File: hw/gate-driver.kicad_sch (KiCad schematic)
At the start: 7 parts

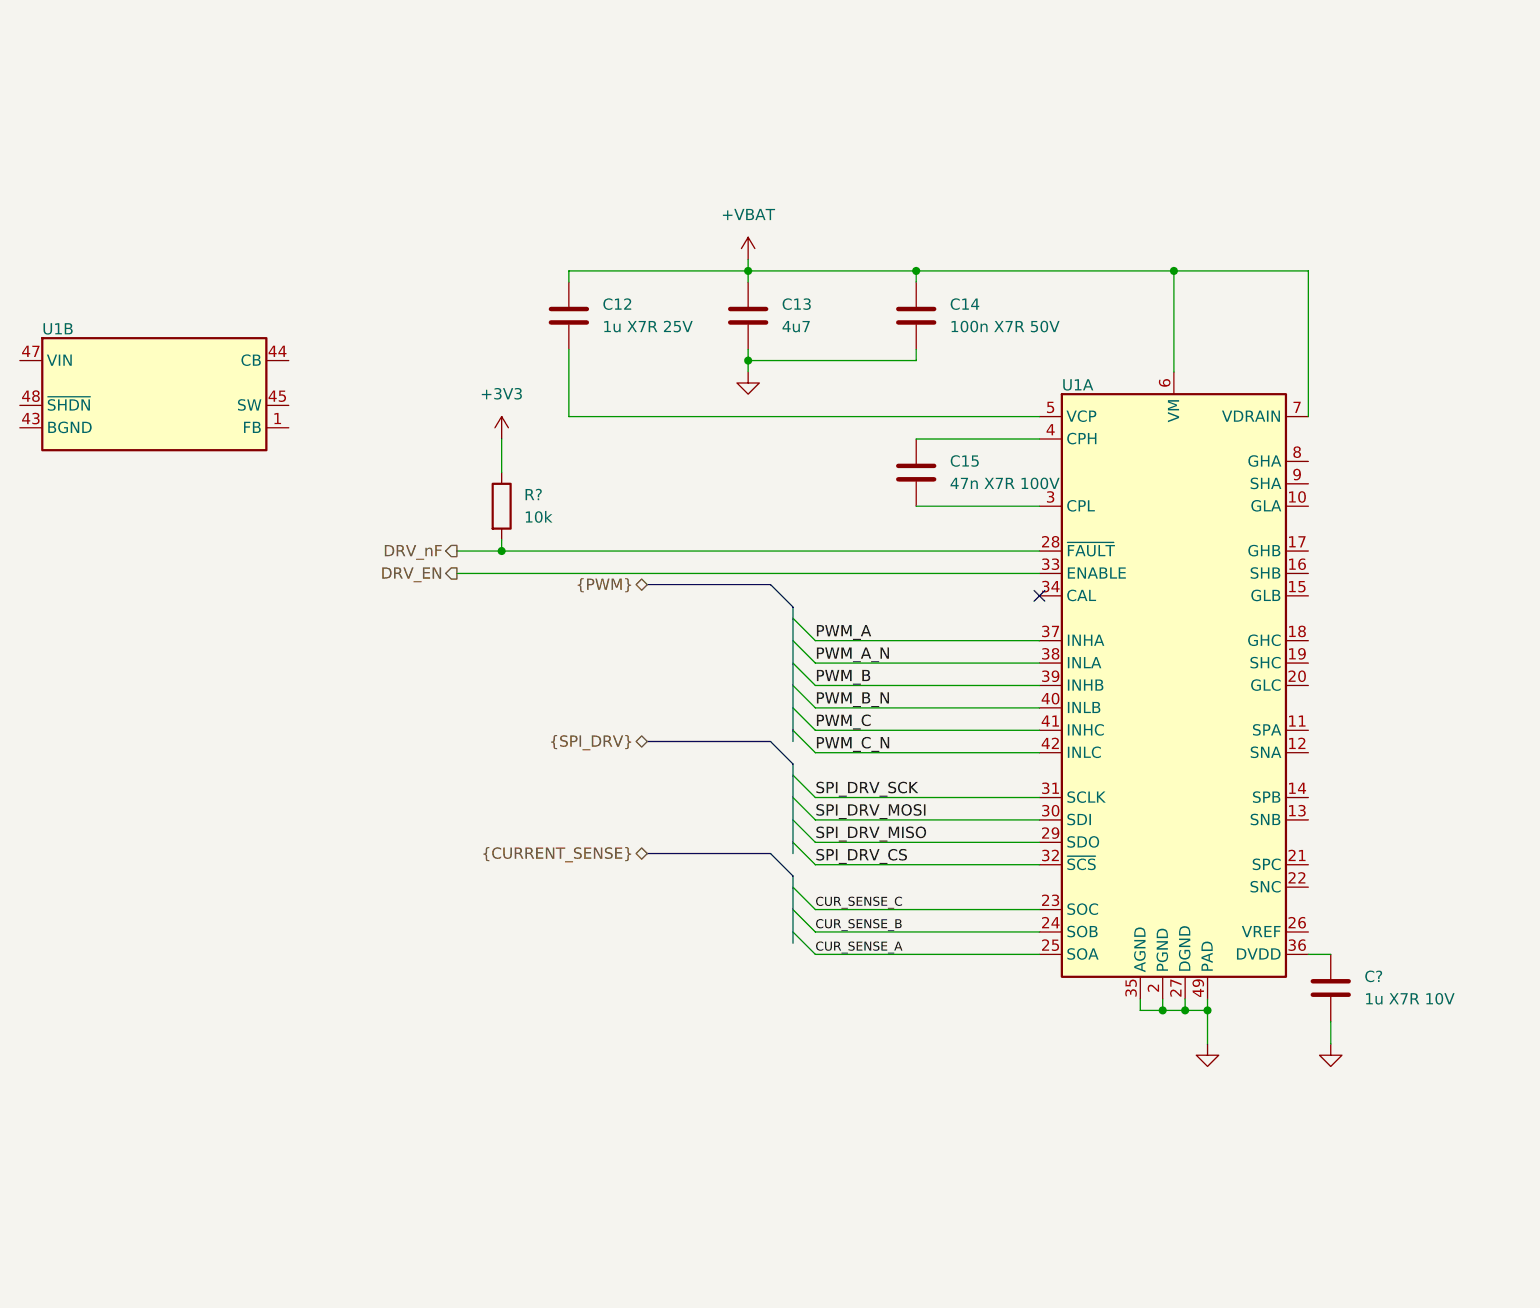
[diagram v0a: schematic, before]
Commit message: add inverter-stage
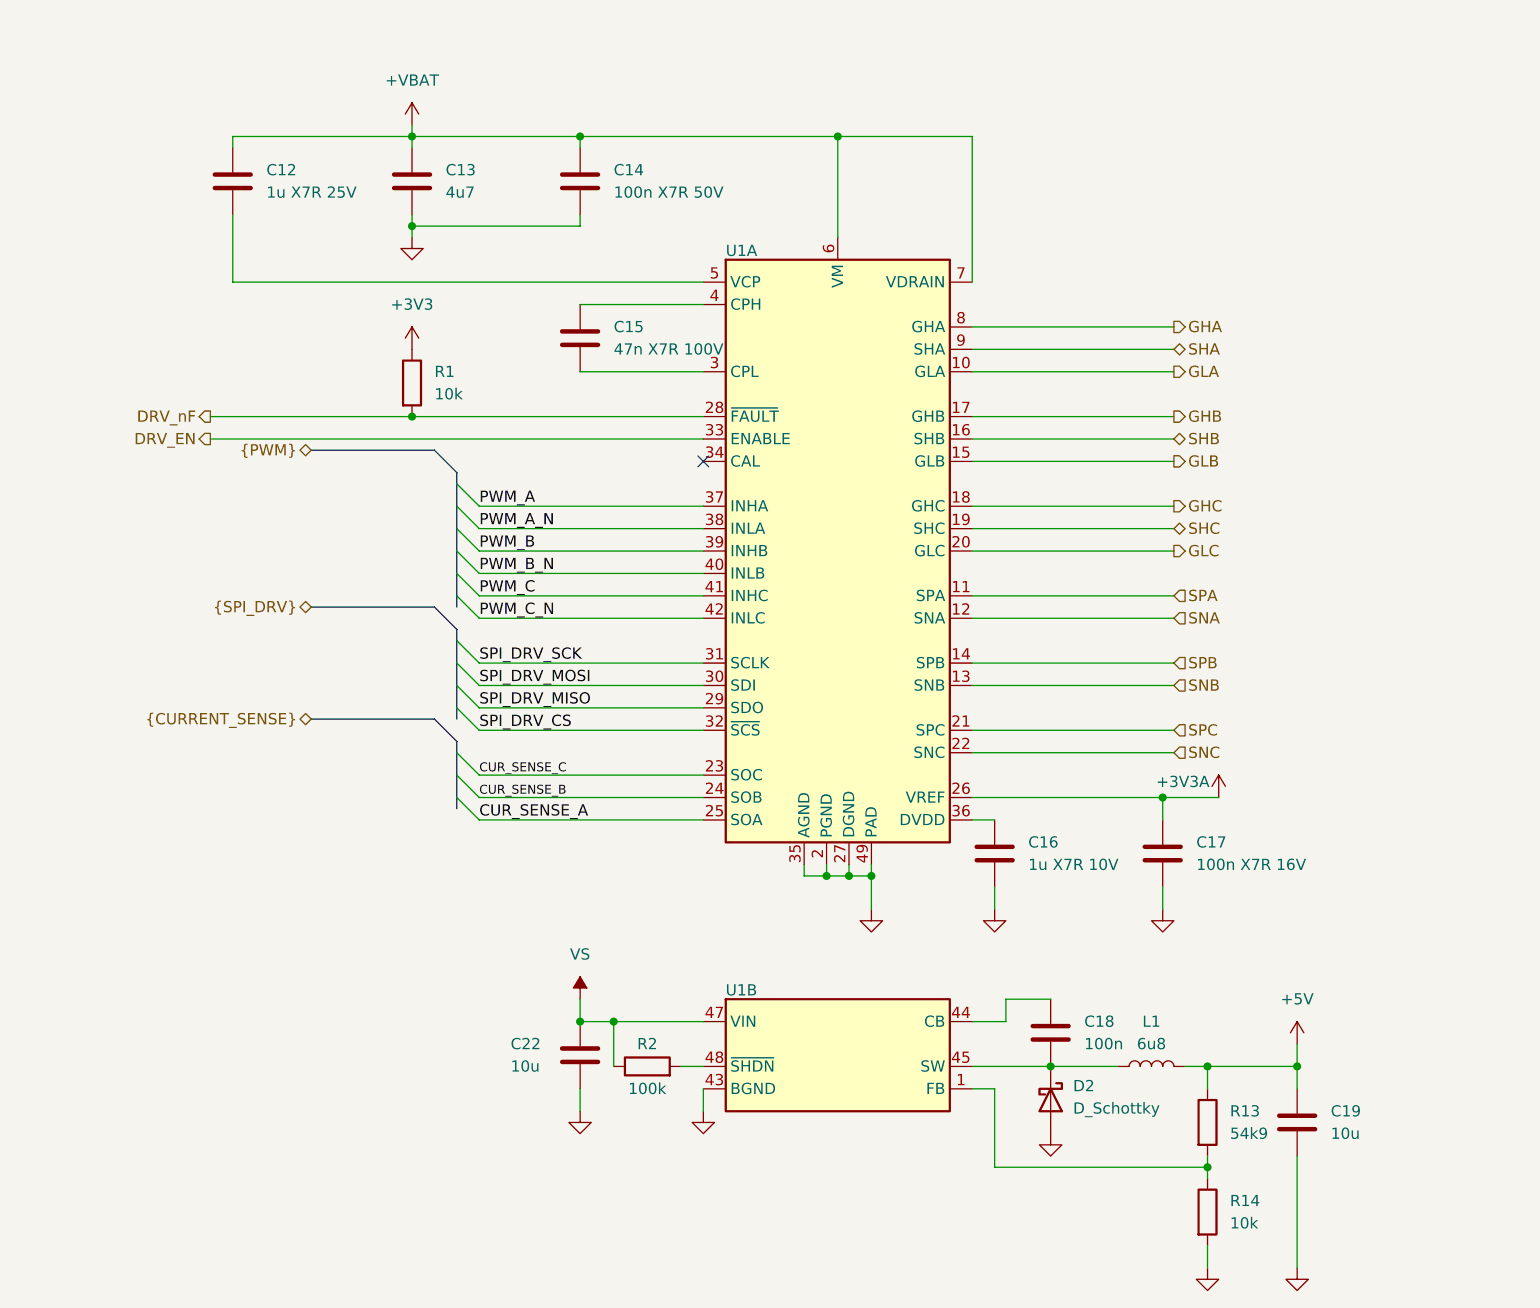
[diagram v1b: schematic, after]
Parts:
- added C17: 100n X7R 16V, symbol Device:C
- added C18: 100n, symbol Device:C
- added C19, C22: 10u, symbol Device:C
- added D2: D_Schottky, symbol Device:D_Schottky
- added L1: 6u8, symbol Device:L
- added R13: 54k9, symbol Device:R
- added R14: 10k, symbol Device:R
- added R2: 100k, symbol Device:R
- gave numbers to parts that had none: 2
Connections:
- net GND: now also U1.43 (BGND), C17.2, C19.2, C22.2, D2.2 (A), R14.2
- net at U1.1 (FB): now also R13.2, R14.1
- net at U1.44 (CB): now also C18.1
- net at U1.45 (SW): now also C18.2, D2.1 (K), L1.1
- net VS: now reaches U1.47 (VIN)
- net VS: now also C22.1, R2.1
- net at U1.48 (~{SHDN}): now also R2.2
- net GLA: now reaches U1.10 (GLA)
- net SPA: now reaches U1.11 (SPA)
- net SNA: now reaches U1.12 (SNA)
- net SNB: now reaches U1.13 (SNB)
- net SPB: now reaches U1.14 (SPB)
- net GLB: now reaches U1.15 (GLB)
- net SHB: now reaches U1.16 (SHB)
- net GHB: now reaches U1.17 (GHB)
- net GHC: now reaches U1.18 (GHC)
- net SHC: now reaches U1.19 (SHC)
- net GLC: now reaches U1.20 (GLC)
- net SPC: now reaches U1.21 (SPC)
- net SNC: now reaches U1.22 (SNC)
- net +3V3A: now reaches U1.26 (VREF)
- net +3V3A: now also C17.1
- net GHA: now reaches U1.8 (GHA)
- net SHA: now reaches U1.9 (SHA)
- new net +5V: C19.1, L1.2, R13.1
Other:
- moved on the sheet: C12, C13, C14, C15, C16, R1, U1A, U1B

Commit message: basic *.kicad_sch done
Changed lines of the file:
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@@
 (kicad_sch
-	(version 20260826)
+	(version 20260830)
 	(generator "eeschema")
 	(generator_version "10.99")
@@
 	)
 	(hierarchical_label "{PWM}"
-		(shape bidirectional)
+		(shape input)
 		(at 92.71 63.5 180)
 		(effects
@@
 	)
 	(hierarchical_label "DRV_EN"
+		(shape input)
+		(at 81.28 62.23 180)
+		(effects
+			(font
+				(size 1.27 1.27)
+			)
+			(justify right)
+		)
+	)
+	(hierarchical_label "{CURRENT_SENSE}"
 		(shape output)
-		(at 81.28 62.23 180)
-		(effects
-			(font
-				(size 1.27 1.27)
-			)
-			(justify right)
-		)
-	)
-	(hierarchical_label "{CURRENT_SENSE}"
-		(shape bidirectional)
 		(at 92.71 93.98 180)
 		(effects

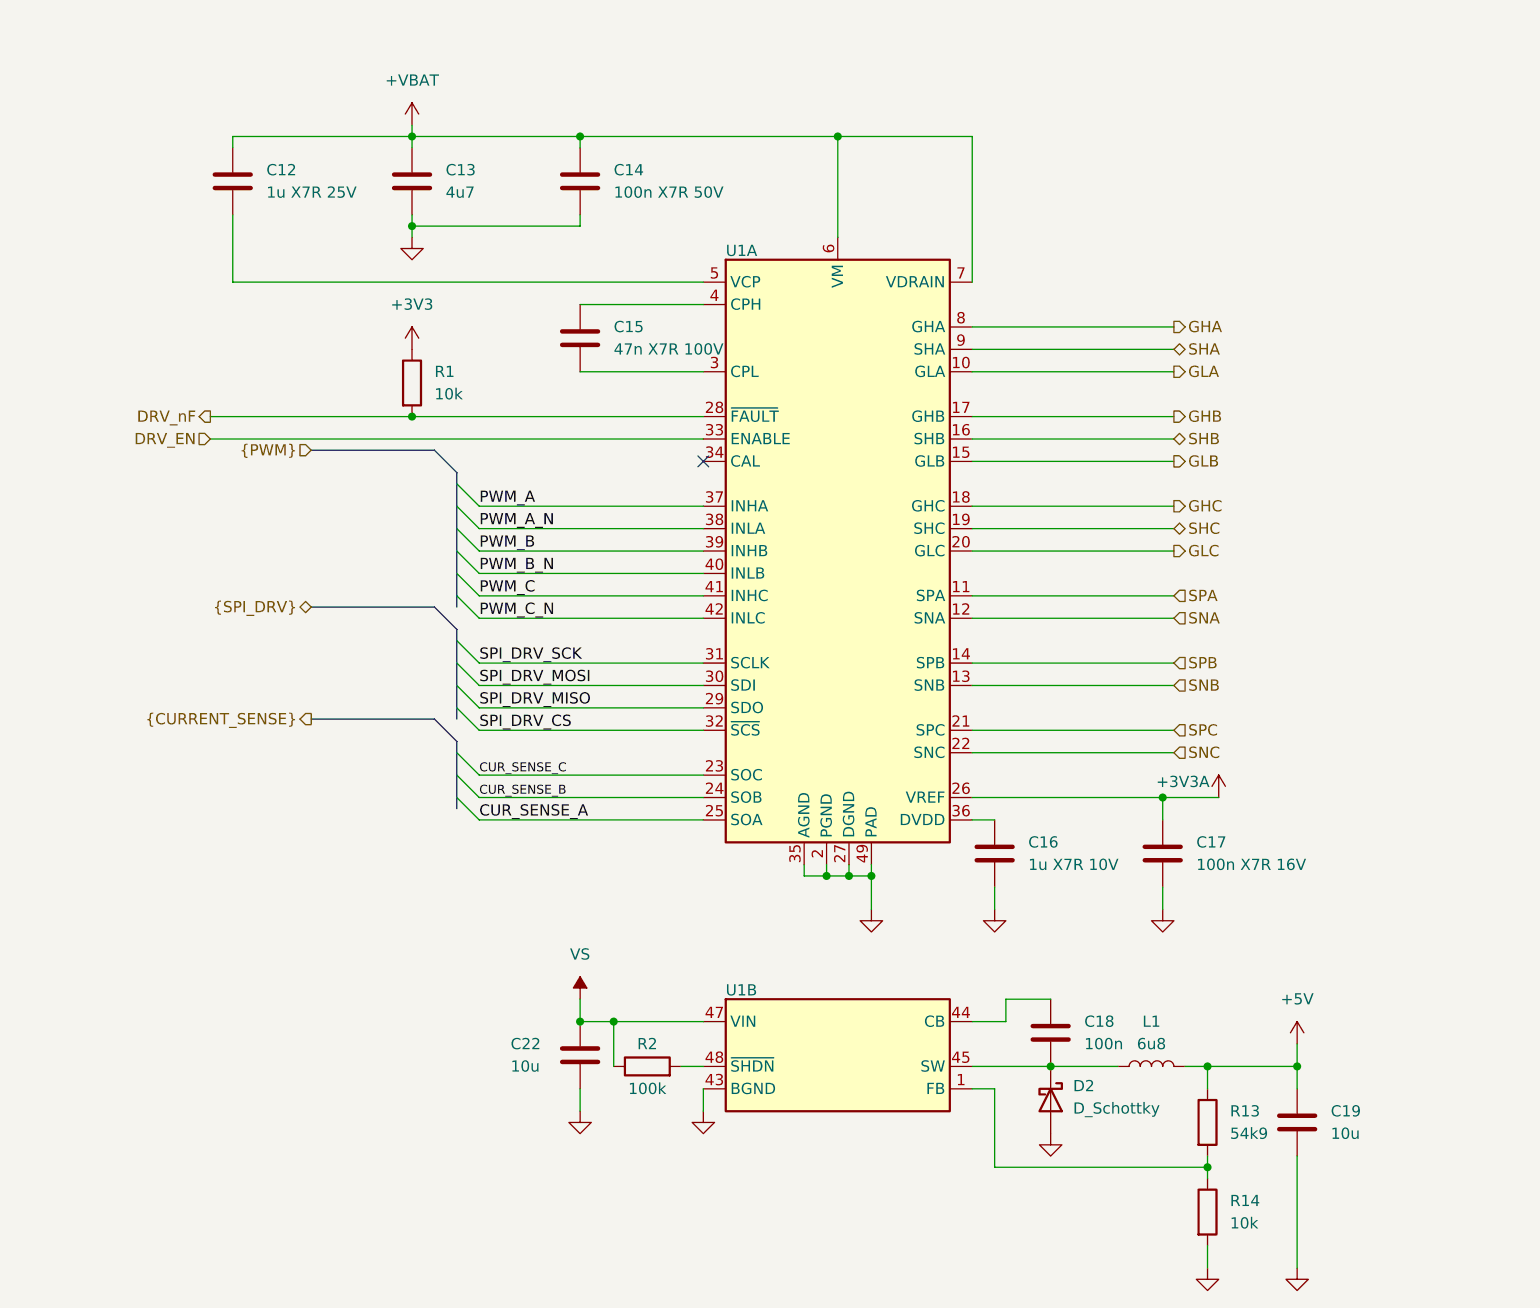
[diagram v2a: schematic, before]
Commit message: began with lcsc and footprints
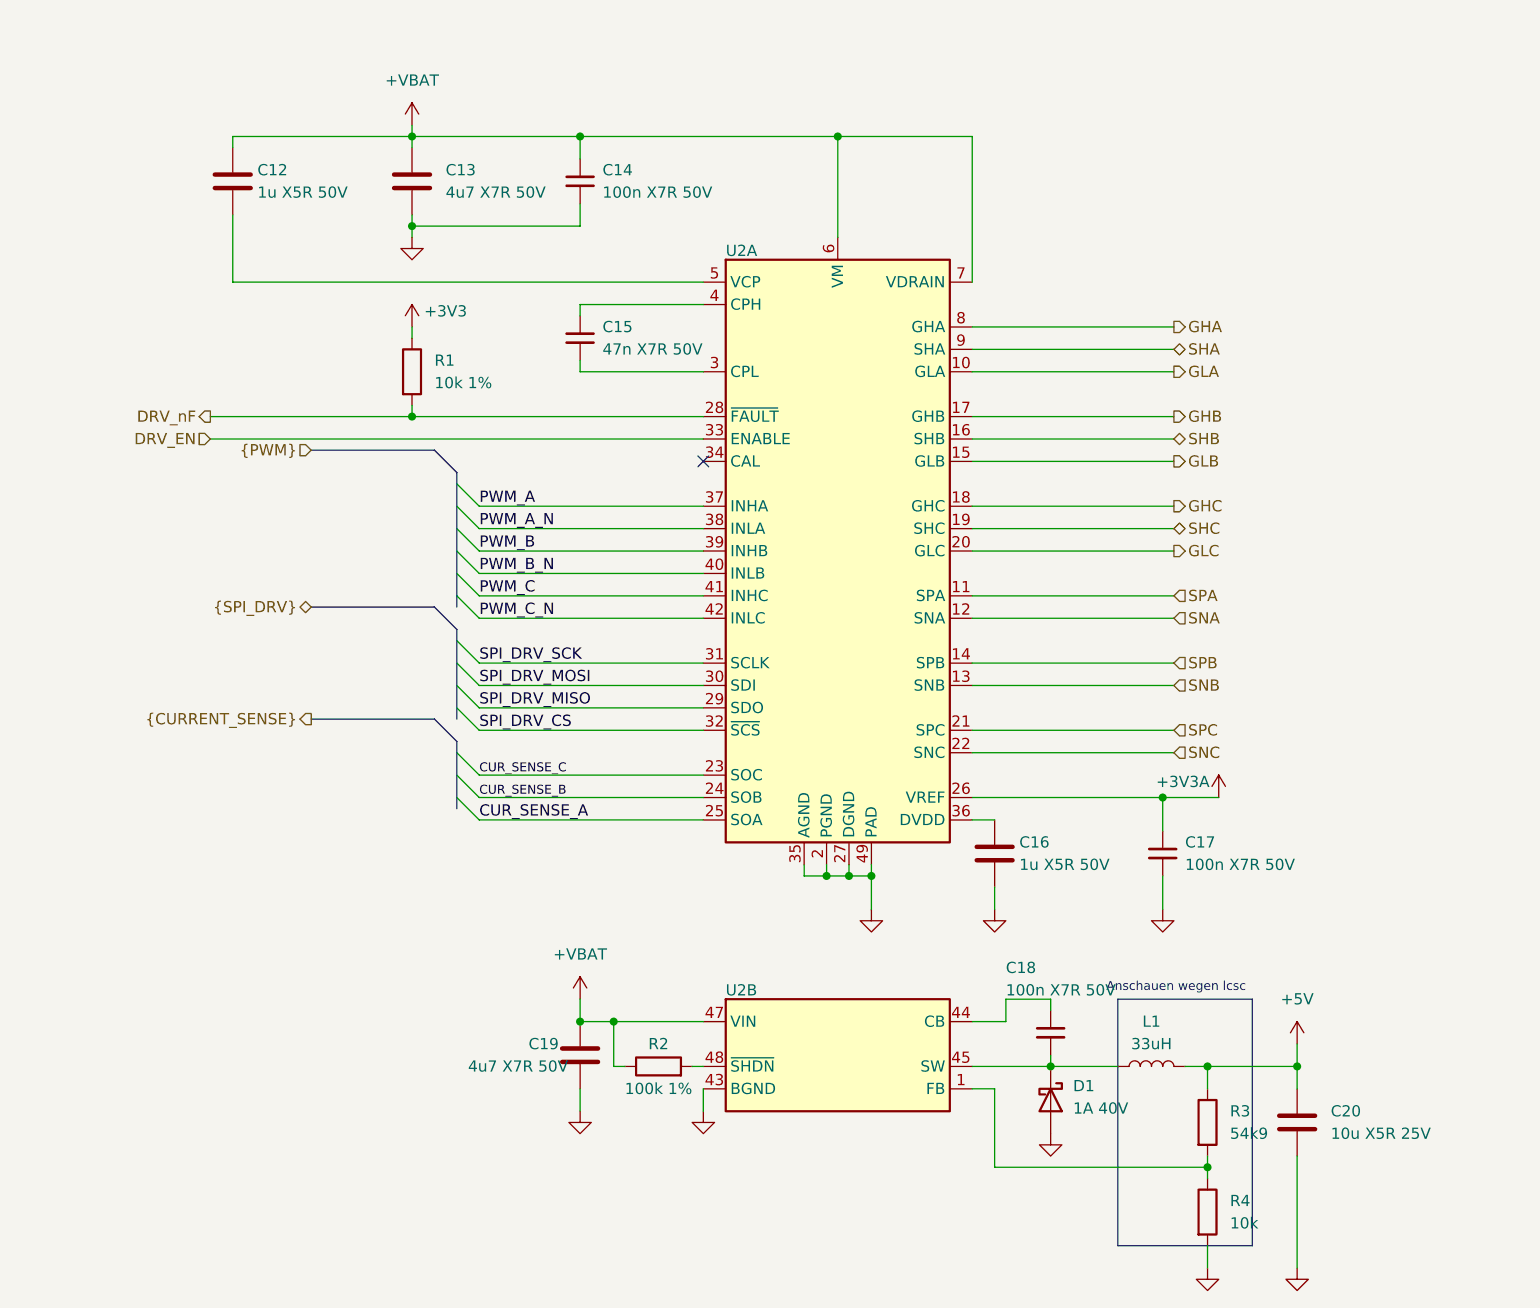
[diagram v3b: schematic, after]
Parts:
- removed C14: 100n X7R 50V, symbol Device:C
- removed C15: 47n X7R 100V, symbol Device:C
- removed C17: 100n X7R 16V, symbol Device:C
- removed C18: 100n, symbol Device:C
- removed C22: 10u, symbol Device:C
- added C14, C17, C18: 100n X7R 50V, Capacitor_SMD:C_0603_1608Metric, symbol Device:C_Small
- added C15: 47n X7R 50V, Capacitor_SMD:C_0603_1608Metric, symbol Device:C_Small
- added C19: 4u7 X7R 50V, Capacitor_SMD:C_1206_3216Metric, symbol Device:C
- C12: value 1u X7R 25V -> 1u X5R 50V; footprint (none) -> Capacitor_SMD:C_0603_1608Metric; LCSC (none) -> C15849
- C13: value 4u7 -> 4u7 X7R 50V; footprint (none) -> Capacitor_SMD:C_1206_3216Metric; LCSC (none) -> C29823
- C16: value 1u X7R 10V -> 1u X5R 50V; footprint (none) -> Capacitor_SMD:C_0603_1608Metric; LCSC (none) -> C15849
- C20: renamed from C19; value 10u -> 10u X5R 25V; footprint (none) -> Capacitor_SMD:C_0805_2012Metric; LCSC (none) -> C15850
- D1: renamed from D2; value D_Schottky -> 1A 40V; footprint (none) -> Diode_SMD:D_SOD-123; LCSC (none) -> C8598
- L1: value 6u8 -> 33uH; footprint (none) -> Inductor_SMD:L_APV_ANR6020; LCSC (none) -> C341059
- R1: value 10k -> 10k 1%; footprint (none) -> Resistor_SMD:R_0603_1608Metric; LCSC (none) -> C25804
- R2: value 100k -> 100k 1%; footprint (none) -> Resistor_SMD:R_0603_1608Metric; LCSC (none) -> C25803
- renumbered R13 to R3, R14 to R4, U1 to U2
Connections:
- net VS is gone; now on net +VBAT: R2.1, U2.47 (VIN)
- net +3V3A: now also C17.1
- net +VBAT: now also C14.1, C19.1
- net GND: now also C14.2, C17.2, C19.2
- net at U2.4 (CPH): now also C15.1
- net at U2.3 (CPL): now also C15.2
- net at U2.44 (CB): now also C18.1
- net at D1.1 (K), L1.1, U2.45 (SW): now also C18.2
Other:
- note added: "Anschauen wegen lcsc"
- moved on the sheet: R1, R2
